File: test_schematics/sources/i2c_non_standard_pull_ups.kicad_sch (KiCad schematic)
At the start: 4 parts, among them U3 STM32F030F4Px, U4 PCA9536DP

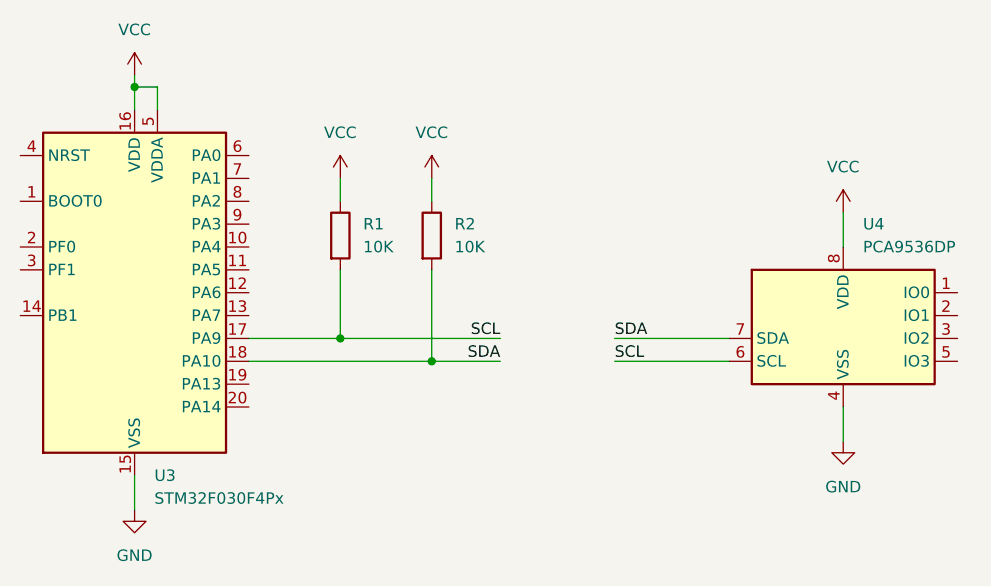
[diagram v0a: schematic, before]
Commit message: refactor: re-annotate test schematics with page X100 designators.
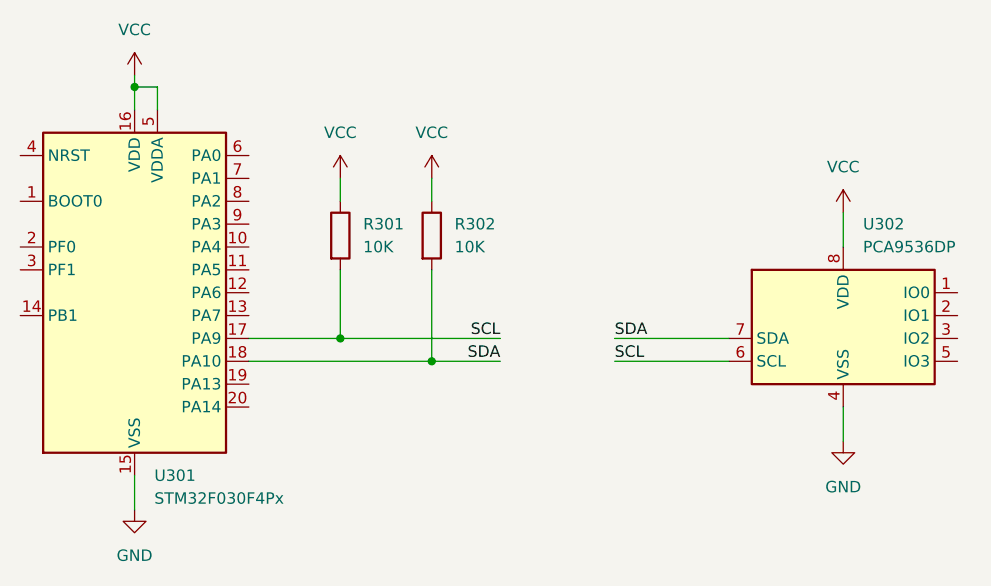
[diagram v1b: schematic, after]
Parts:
- renumbered R1 to R301, R2 to R302, U3 to U301, U4 to U302
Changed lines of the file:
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@@
 		(dnp no)
 		(fields_autoplaced yes)
-		(property "Reference" "#PWR07"
+		(property "Reference" "#PWR0305"
 			(at 152.4 63.5 0)
 			(effects
@@
 			(project "test_schematics"
 				(path "/f327a4b6-22d9-4671-bd1f-2c46b703509e/1284c5bc-3fac-4644-8578-1906a627e12f"
-					(reference "#PWR07")
+					(reference "#PWR0305")
 					(unit 1)
 				)
@@
 		(dnp no)
 		(fields_autoplaced yes)
-		(property "Reference" "U3"
+		(property "Reference" "U301"
 			(at 75.8541 88.9 0)
 			(effects
@@
 			(project "test_schematics"
 				(path "/f327a4b6-22d9-4671-bd1f-2c46b703509e/1284c5bc-3fac-4644-8578-1906a627e12f"
-					(reference "U3")
+					(reference "U301")
 					(unit 1)
 				)
@@
 		(dnp no)
 		(fields_autoplaced yes)
-		(property "Reference" "#PWR05"
+		(property "Reference" "#PWR0301"
 			(at 73.66 48.26 0)
 			(effects
@@
 			(project "test_schematics"
 				(path "/f327a4b6-22d9-4671-bd1f-2c46b703509e/1284c5bc-3fac-4644-8578-1906a627e12f"
-					(reference "#PWR05")
+					(reference "#PWR0301")
 					(unit 1)
 				)
@@
 		(dnp no)
 		(fields_autoplaced yes)
-		(property "Reference" "R1"
+		(property "Reference" "R301"
 			(at 99.06 60.9599 0)
 			(effects
@@
 			(project ""
 				(path "/f327a4b6-22d9-4671-bd1f-2c46b703509e/1284c5bc-3fac-4644-8578-1906a627e12f"
-					(reference "R1")
+					(reference "R301")
 					(unit 1)
 				)
@@
 		(dnp no)
 		(fields_autoplaced yes)
-		(property "Reference" "U4"
+		(property "Reference" "U302"
 			(at 154.5941 60.96 0)
 			(effects
@@
 			(project "test_schematics"
 				(path "/f327a4b6-22d9-4671-bd1f-2c46b703509e/1284c5bc-3fac-4644-8578-1906a627e12f"
-					(reference "U4")
+					(reference "U302")
 					(unit 1)
 				)
@@
 		(dnp no)
 		(fields_autoplaced yes)
-		(property "Reference" "#PWR010"
+		(property "Reference" "#PWR0304"
 			(at 106.68 59.69 0)
 			(effects
@@
 			(project "test_schematics"
 				(path "/f327a4b6-22d9-4671-bd1f-2c46b703509e/1284c5bc-3fac-4644-8578-1906a627e12f"
-					(reference "#PWR010")
+					(reference "#PWR0304")
 					(unit 1)
 				)
@@
 		(dnp no)
 		(fields_autoplaced yes)
-		(property "Reference" "#PWR06"
+		(property "Reference" "#PWR0302"
 			(at 73.66 99.06 0)
 			(effects
@@
 			(project "test_schematics"
 				(path "/f327a4b6-22d9-4671-bd1f-2c46b703509e/1284c5bc-3fac-4644-8578-1906a627e12f"
-					(reference "#PWR06")
+					(reference "#PWR0302")
 					(unit 1)
 				)
@@
 		(dnp no)
 		(fields_autoplaced yes)
-		(property "Reference" "#PWR09"
+		(property "Reference" "#PWR0303"
 			(at 96.52 59.69 0)
 			(effects
@@
 			(project "test_schematics"
 				(path "/f327a4b6-22d9-4671-bd1f-2c46b703509e/1284c5bc-3fac-4644-8578-1906a627e12f"
-					(reference "#PWR09")
+					(reference "#PWR0303")
 					(unit 1)
 				)
@@
 		(dnp no)
 		(fields_autoplaced yes)
-		(property "Reference" "R2"
+		(property "Reference" "R302"
 			(at 109.22 60.9599 0)
 			(effects
@@
 			(project "test_schematics"
 				(path "/f327a4b6-22d9-4671-bd1f-2c46b703509e/1284c5bc-3fac-4644-8578-1906a627e12f"
-					(reference "R2")
+					(reference "R302")
 					(unit 1)
 				)
@@
 		(dnp no)
 		(fields_autoplaced yes)
-		(property "Reference" "#PWR08"
+		(property "Reference" "#PWR0306"
 			(at 152.4 91.44 0)
 			(effects
@@
 			(project "test_schematics"
 				(path "/f327a4b6-22d9-4671-bd1f-2c46b703509e/1284c5bc-3fac-4644-8578-1906a627e12f"
-					(reference "#PWR08")
-					(unit 1)
-				)
+					(reference "#PWR0306")
+					(unit 1)
+				)

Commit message: feat: I2C non-standard pull-ups check
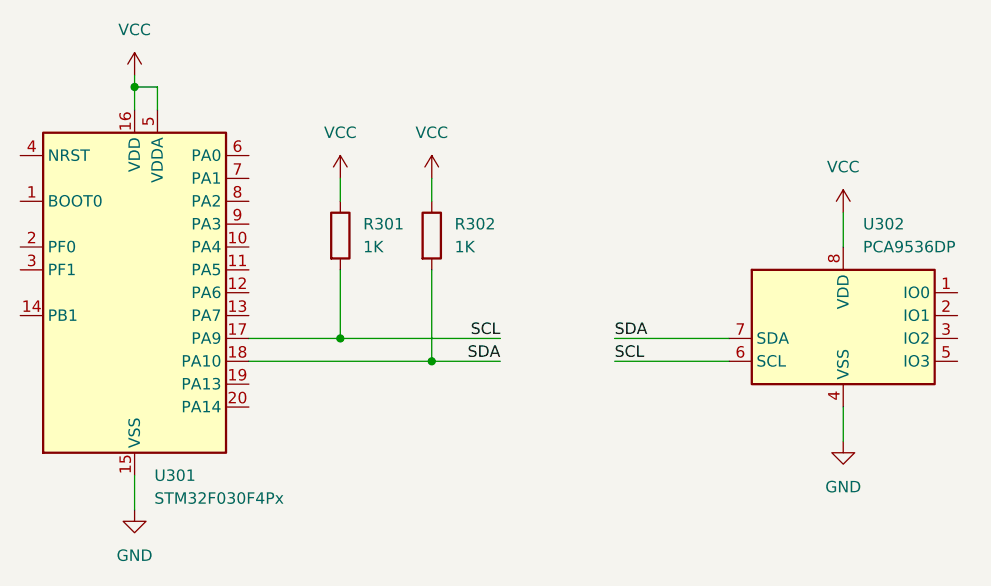
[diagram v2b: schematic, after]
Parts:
- R301, R302: value 10K -> 1K
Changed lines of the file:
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@@
 			)
 		)
-		(property "Value" "10K"
+		(property "Value" "1K"
 			(at 99.06 63.4999 0)
 			(effects
@@
 			)
 		)
-		(property "Value" "10K"
+		(property "Value" "1K"
 			(at 109.22 63.4999 0)
 			(effects
